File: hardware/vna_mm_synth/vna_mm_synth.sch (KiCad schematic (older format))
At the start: 0 parts

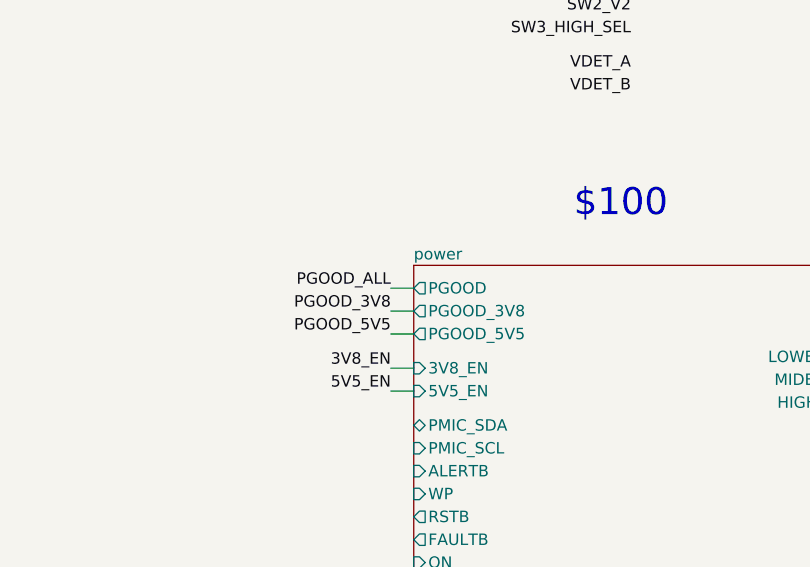
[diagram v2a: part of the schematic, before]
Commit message: fixed mirrored 3.3V regulator on sequencer board, created and assigned footprints for synth
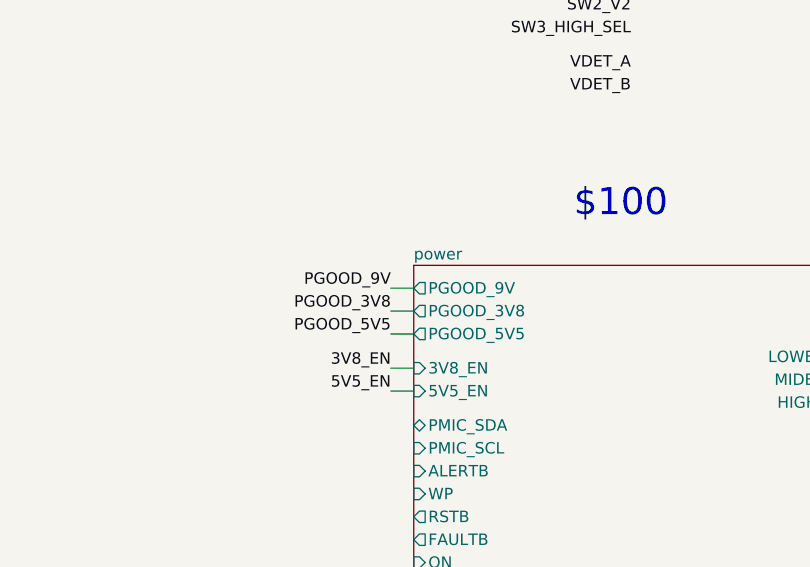
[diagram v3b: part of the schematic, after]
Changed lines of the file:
@@
 F10 "MIDBAND_EN" I L 6950 9450 50
 F11 "HIGHBAND_EN" I L 6950 9550 50
-F12 "PGOOD" O L 6950 7900 50
-F13 "PMIC_SDA" B L 6950 8500 50
-F14 "PMIC_SCL" I L 6950 8600 50
-F15 "ALERTB" I L 6950 8700 50
-F16 "WP" I L 6950 8800 50
-F17 "RSTB" O L 6950 8900 50
-F18 "FAULTB" O L 6950 9000 50
-F19 "ON" I L 6950 9100 50
-F20 "PMIC_3V3" O L 6950 9200 50
+F12 "PMIC_SDA" B L 6950 8500 50
+F13 "PMIC_SCL" I L 6950 8600 50
+F14 "ALERTB" I L 6950 8700 50
+F15 "WP" I L 6950 8800 50
+F16 "RSTB" O L 6950 8900 50
+F17 "FAULTB" O L 6950 9000 50
+F18 "ON" I L 6950 9100 50
+F19 "PMIC_3V3" O L 6950 9200 50
+F20 "PGOOD_9V" O L 6950 7900 50
 $EndSheet
 Wire Wire Line
@@
 	10750 9850 10600 9850
 Text Label 6850 7900 2    50   ~ 0
-PGOOD_ALL
+PGOOD_9V
 Wire Wire Line
 	6850 7900 6950 7900

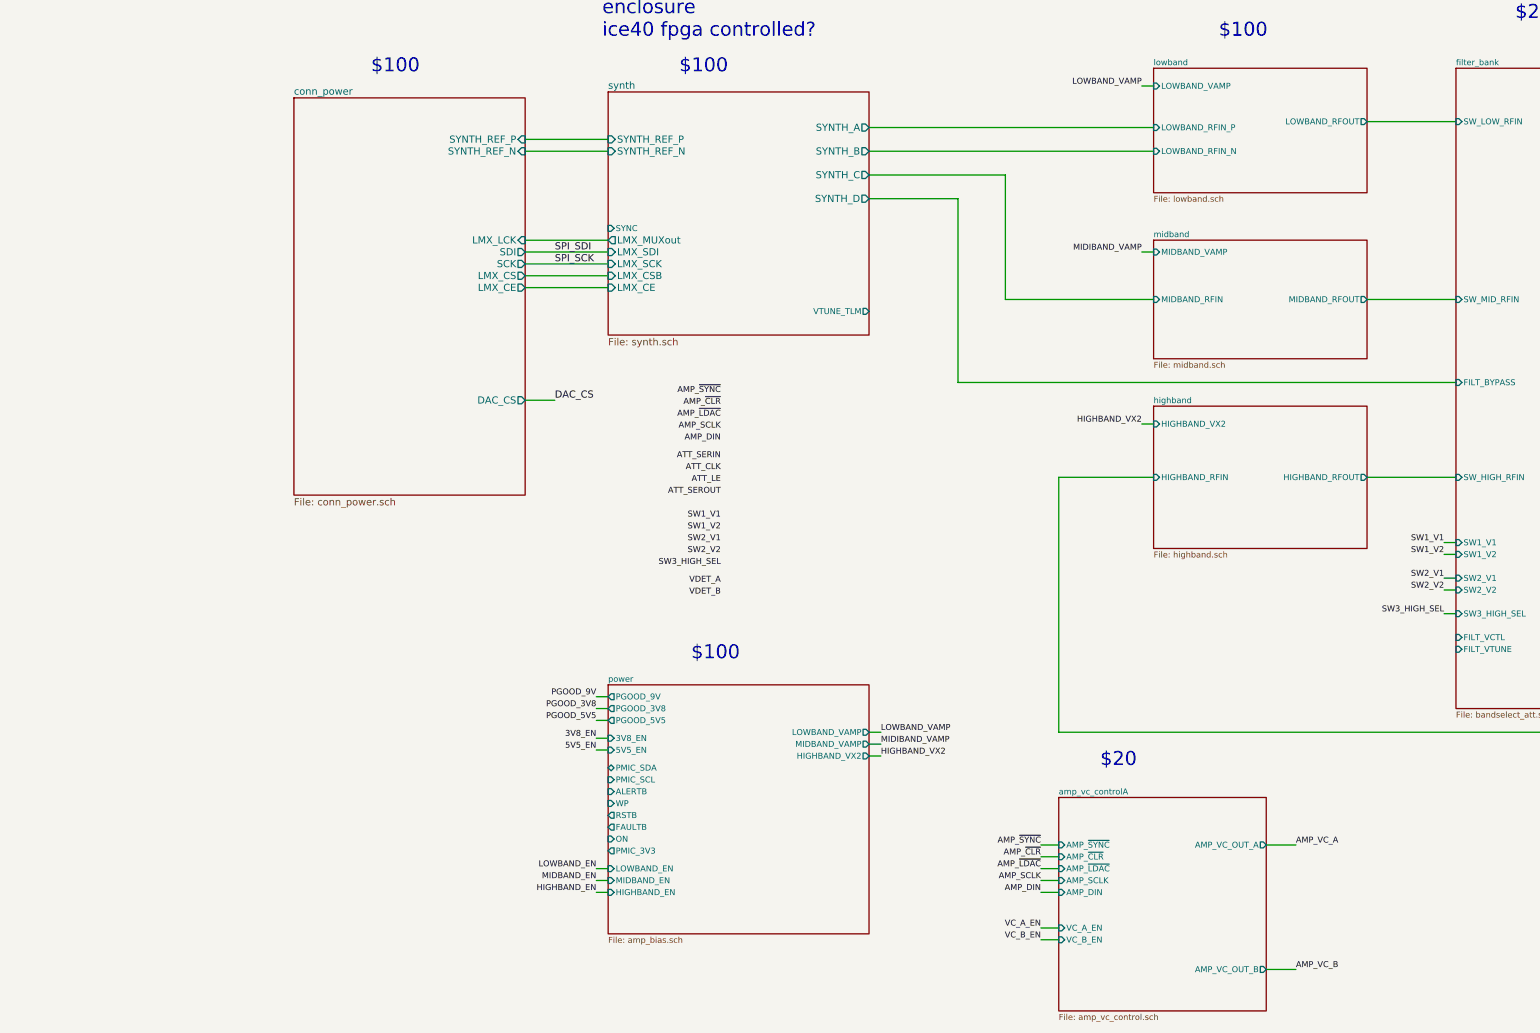
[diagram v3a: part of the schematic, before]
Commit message: started variable filter bias circuitry - added 15V bias
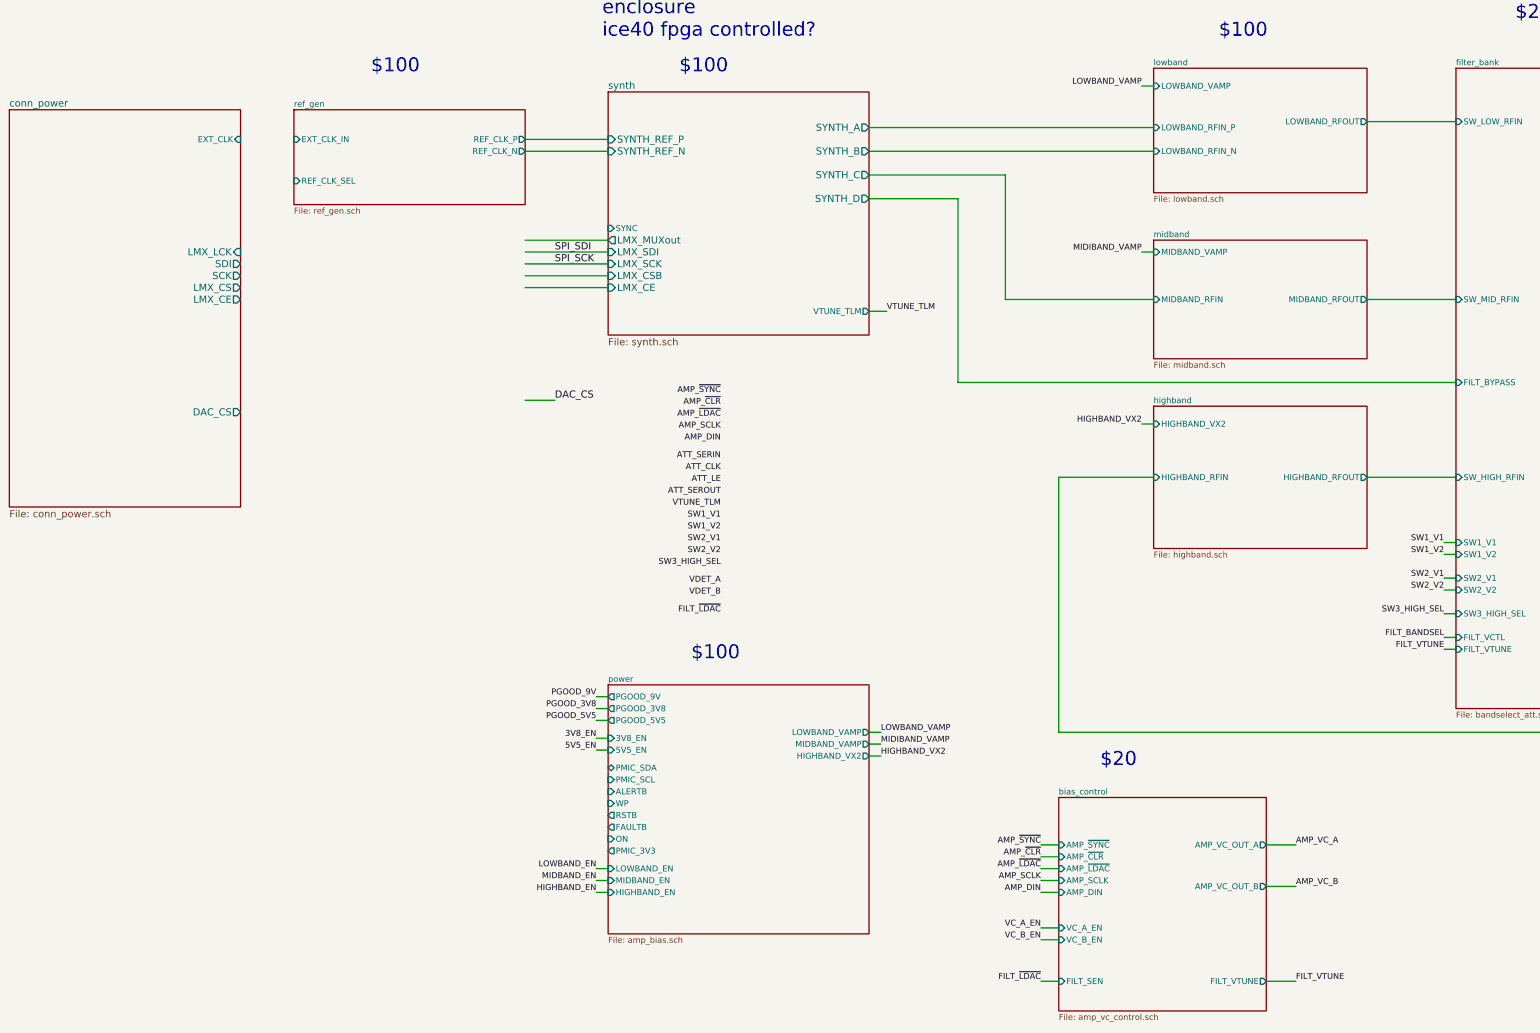
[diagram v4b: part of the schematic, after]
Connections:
- net labels added: FILT_BANDSEL, FILT_VTUNE, FILT_~LDAC, VTUNE_TLM
- wire segments 63 -> 68
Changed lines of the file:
@@
 $Descr C 22000 17000
 encoding utf-8
-Sheet 1 11
+Sheet 1 12
 Title ""
 Date ""
@@
 $EndDescr
 $Sheet
-S 4300 2850 1950 3350
+S 1900 2950 1950 3350
 U 5AB8DC0D
 F0 "conn_power" 60
 F1 "conn_power.sch" 60
-F2 "SYNTH_REF_P" I R 6250 3200 60
-F3 "SYNTH_REF_N" I R 6250 3300 60
-F4 "SDI" O R 6250 4150 60
-F5 "SCK" O R 6250 4250 60
-F6 "LMX_CS" O R 6250 4350 60
-F7 "DAC_CS" O R 6250 5400 60
-F8 "LMX_CE" O R 6250 4450 60
-F9 "LMX_LCK" I R 6250 4050 60
+F2 "SDI" O R 3850 4250 60
+F3 "SCK" O R 3850 4350 60
+F4 "LMX_CS" O R 3850 4450 60
+F5 "DAC_CS" O R 3850 5500 60
+F6 "LMX_CE" O R 3850 4550 60
+F7 "LMX_LCK" I R 3850 4150 60
+F8 "EXT_CLK" I R 3850 3200 50
 $EndSheet
 $Sheet
@@
 Text Label 12750 9150 0    50   ~ 0
 AMP_VC_A
-Text Label 12750 10200 0    50   ~ 0
+Text Label 12750 9500 0    50   ~ 0
 AMP_VC_B
 Text Label 11450 2750 2    50   ~ 0
@@
 S 10750 8750 1750 1800
 U 5D8E086E
-F0 "amp_vc_controlA" 50
+F0 "bias_control" 50
 F1 "amp_vc_control.sch" 50
 F2 "AMP_VC_OUT_A" O R 12500 9150 50
@@
 F6 "AMP_SCLK" I L 10750 9450 50
 F7 "AMP_DIN" I L 10750 9550 50
-F8 "AMP_VC_OUT_B" O R 12500 10200 50
+F8 "AMP_VC_OUT_B" O R 12500 9500 50
 F9 "VC_B_EN" I L 10750 9950 50
 F10 "VC_A_EN" I L 10750 9850 50
+F11 "FILT_VTUNE" O R 12500 10300 50
+F12 "FILT_SEN" I L 10750 10300 50
 $EndSheet
 Wire Wire Line
 	12500 9150 12750 9150
 Wire Wire Line
-	12500 10200 12750 10200
+	12500 9500 12750 9500
 $Sheet
 S 6950 7800 2200 2100
@@
 Wire Wire Line
 	9900 5250 9900 3700
+Wire Wire Line
+	9150 4650 9300 4650
+Text Label 9300 4650 0    50   ~ 0
+VTUNE_TLM
+Text Label 7900 6300 2    50   ~ 0
+VTUNE_TLM
+$Sheet
+S 4300 2950 1950 800
+U 5DB13A27
+F0 "ref_gen" 50
+F1 "ref_gen.sch" 50
+F2 "REF_CLK_P" O R 6250 3200 50
+F3 "REF_CLK_N" O R 6250 3300 50
+F4 "EXT_CLK_IN" I L 4300 3200 50
+F5 "REF_CLK_SEL" I L 4300 3550 50
+$EndSheet
+Wire Wire Line
+	12500 10300 12750 10300
+Text Label 12750 10300 0    50   ~ 0
+FILT_VTUNE
+Text Label 14000 7500 2    50   ~ 0
+FILT_VTUNE
+Text Label 14000 7400 2    50   ~ 0
+FILT_BANDSEL
+Wire Wire Line
+	14000 7400 14100 7400
+Wire Wire Line
+	14000 7500 14100 7500
+Wire Wire Line
+	10750 10300 10600 10300
+Text Label 10600 10300 2    50   ~ 0
+FILT_~LDAC
+Text Label 7900 7200 2    50   ~ 0
+FILT_~LDAC
 $EndSCHEMATC

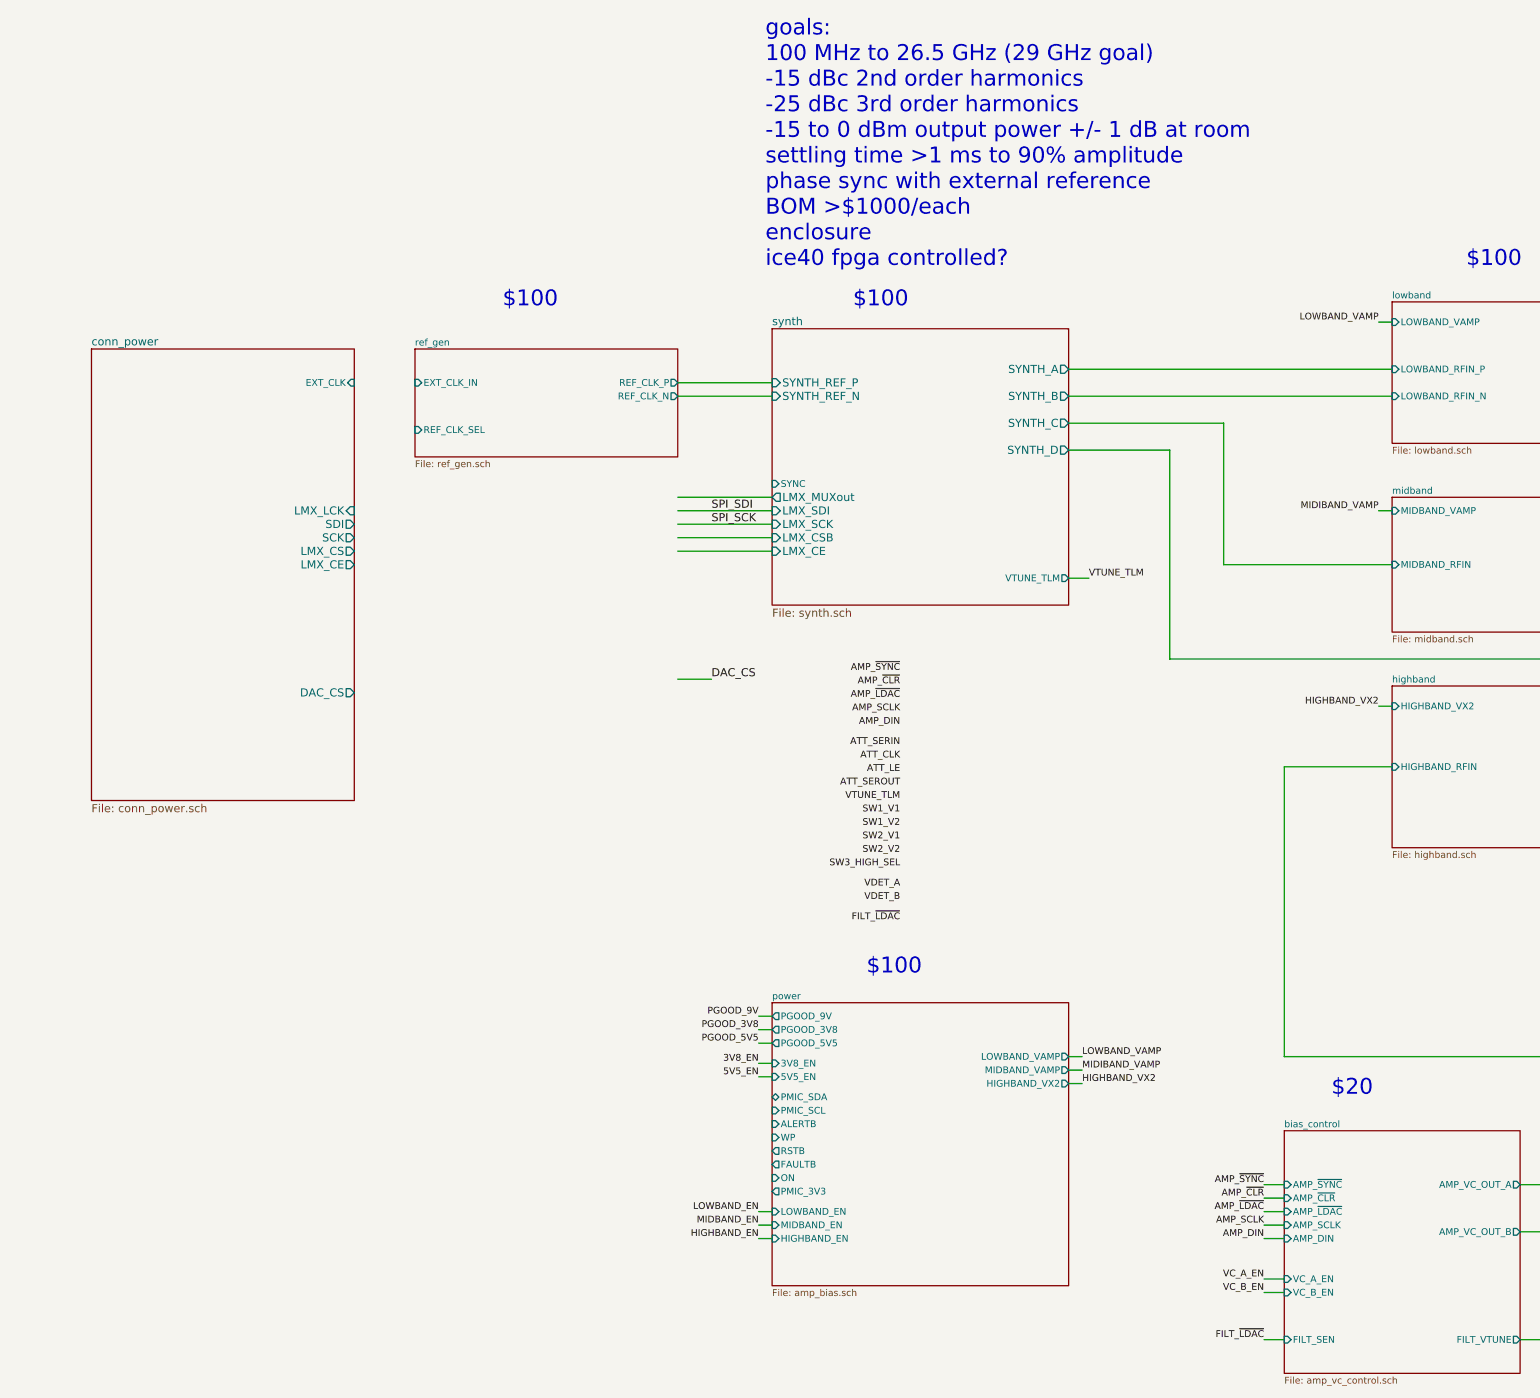
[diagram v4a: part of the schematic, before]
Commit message: started separate reference clock generation board
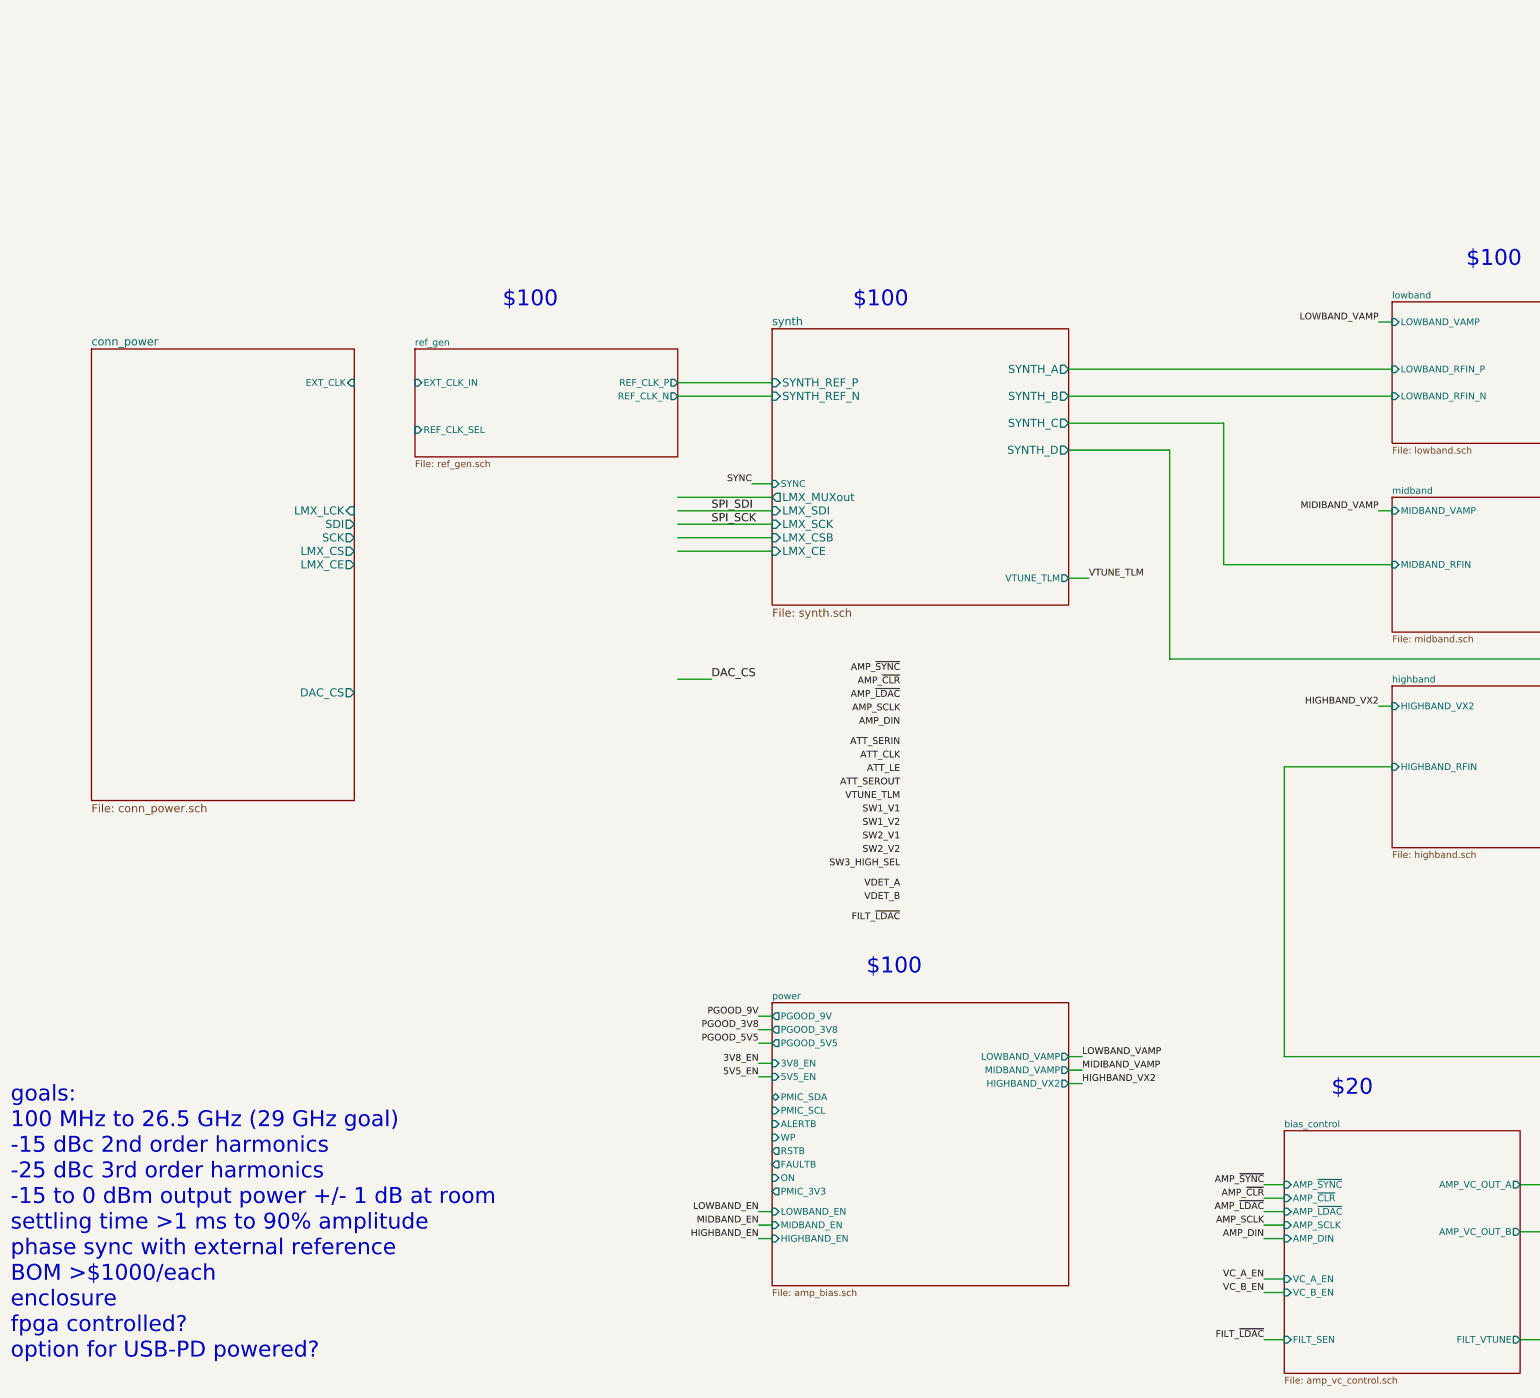
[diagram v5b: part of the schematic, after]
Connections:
- wire segments 68 -> 69
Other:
- note added: "goals:\n100 MHz to 26.5 GHz (29 GHz goal)\n-15 dBc 2nd order harmonics\n-25 dBc 3rd order harmonics\n-15 to 0 dBm output power +/- 1 dB at room\nsettling time >1 ms to 90% amplitude\nphase sync with external reference\nBOM >$1000/each\nenclosure\nfpga controlled?\noption for USB-PD powered?"
- note removed: "goals:\n100 MHz to 26.5 GHz (29 GHz goal)\n-15 dBc 2nd order harmonics\n-25 dBc 3rd order harmonics\n-15 to 0 dBm output power +/- 1 dB at room\nsettling time >1 ms to 90% amplitude\nphase sync with external reference\nBOM >$1000/each\nenclosure\nice40 fpga controlled?"
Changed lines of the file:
@@
 F4 "HIGHBAND_RFIN" I L 11550 6050 50
 $EndSheet
-Text Notes 6900 2350 0    118  ~ 0
-goals:\n100 MHz to 26.5 GHz (29 GHz goal)\n-15 dBc 2nd order harmonics\n-25 dBc 3rd order harmonics\n-15 to 0 dBm output power +/- 1 dB at room\nsettling time >1 ms to 90% amplitude\nphase sync with external reference\nBOM >$1000/each\nenclosure\nice40 fpga controlled?
+Text Notes 1300 10450 0    118  ~ 0
+goals:\n100 MHz to 26.5 GHz (29 GHz goal)\n-15 dBc 2nd order harmonics\n-25 dBc 3rd order harmonics\n-15 to 0 dBm output power +/- 1 dB at room\nsettling time >1 ms to 90% amplitude\nphase sync with external reference\nBOM >$1000/each\nenclosure\nfpga controlled?\noption for USB-PD powered?
 Wire Wire Line
 	11550 6050 10750 6050
@@
 Text Label 7900 7200 2    50   ~ 0
 FILT_~LDAC
+Text Label 6800 3950 2    50   ~ 0
+SYNC
+Wire Wire Line
+	6800 3950 6950 3950
 $EndSCHEMATC
